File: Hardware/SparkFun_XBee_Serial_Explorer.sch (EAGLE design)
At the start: 45 parts, among them Q1 MBT2222, U1 MAX232SOIC16, U2 XBEE-1B3, U3 LM117

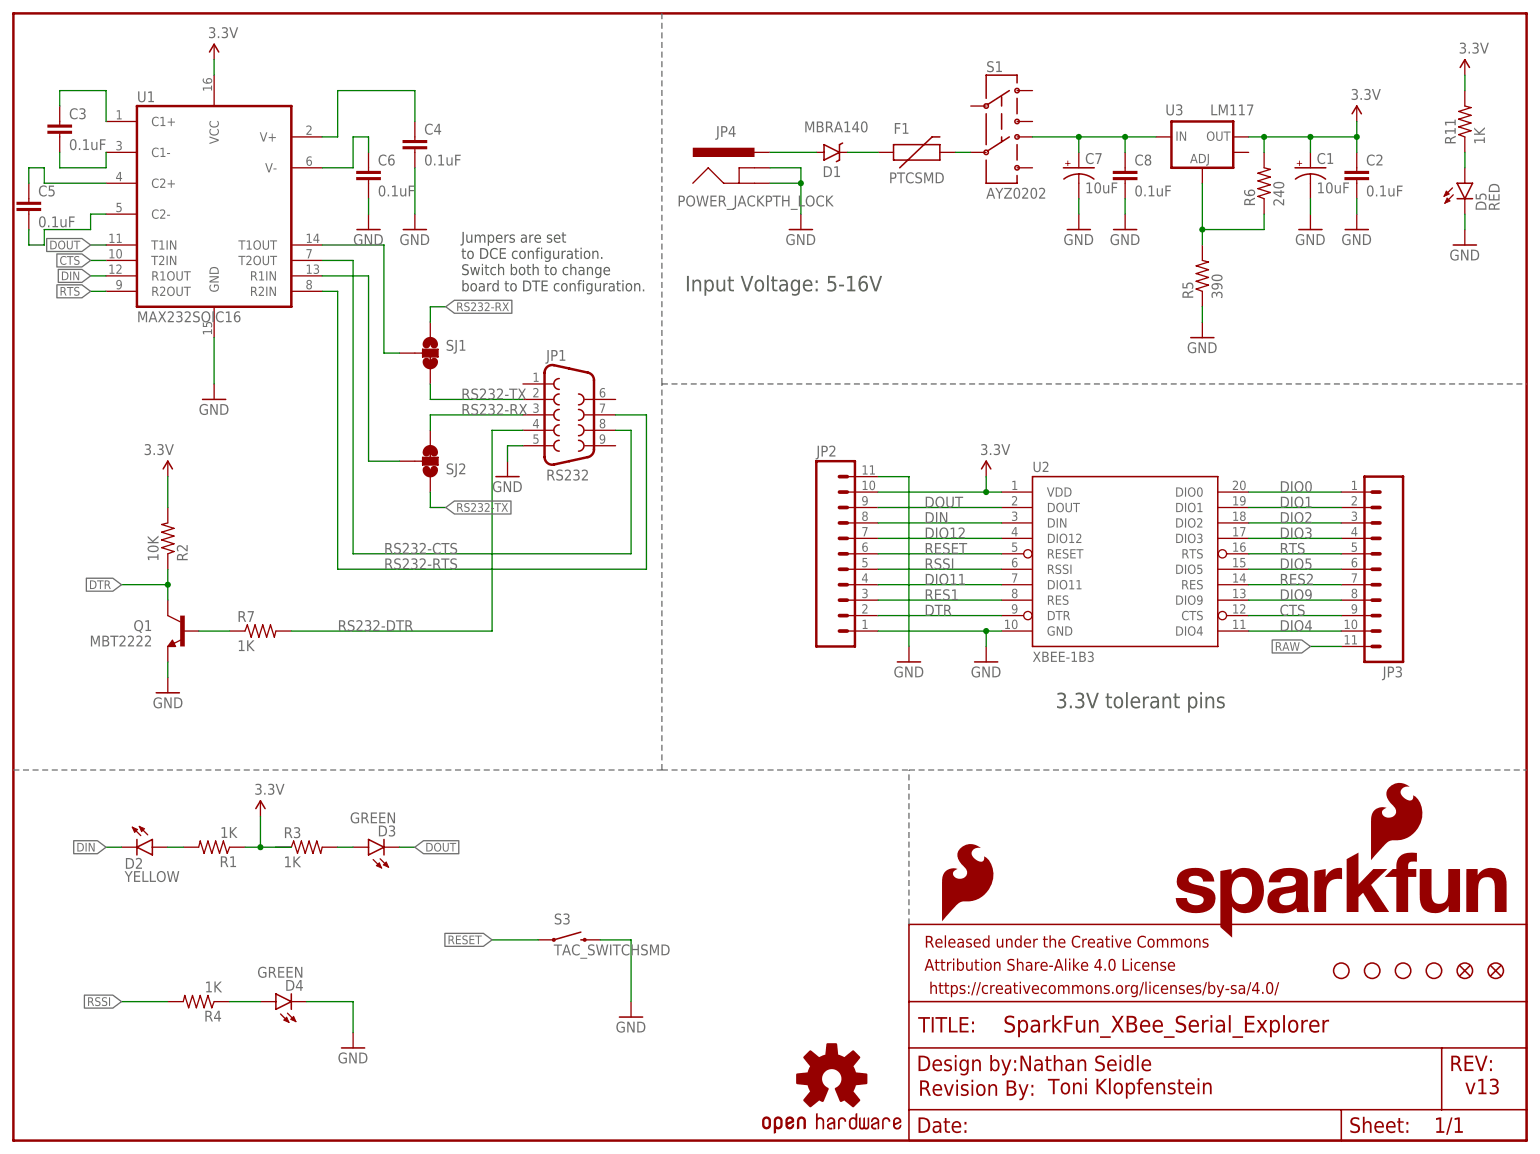
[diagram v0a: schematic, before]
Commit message: Adding in test points for QC
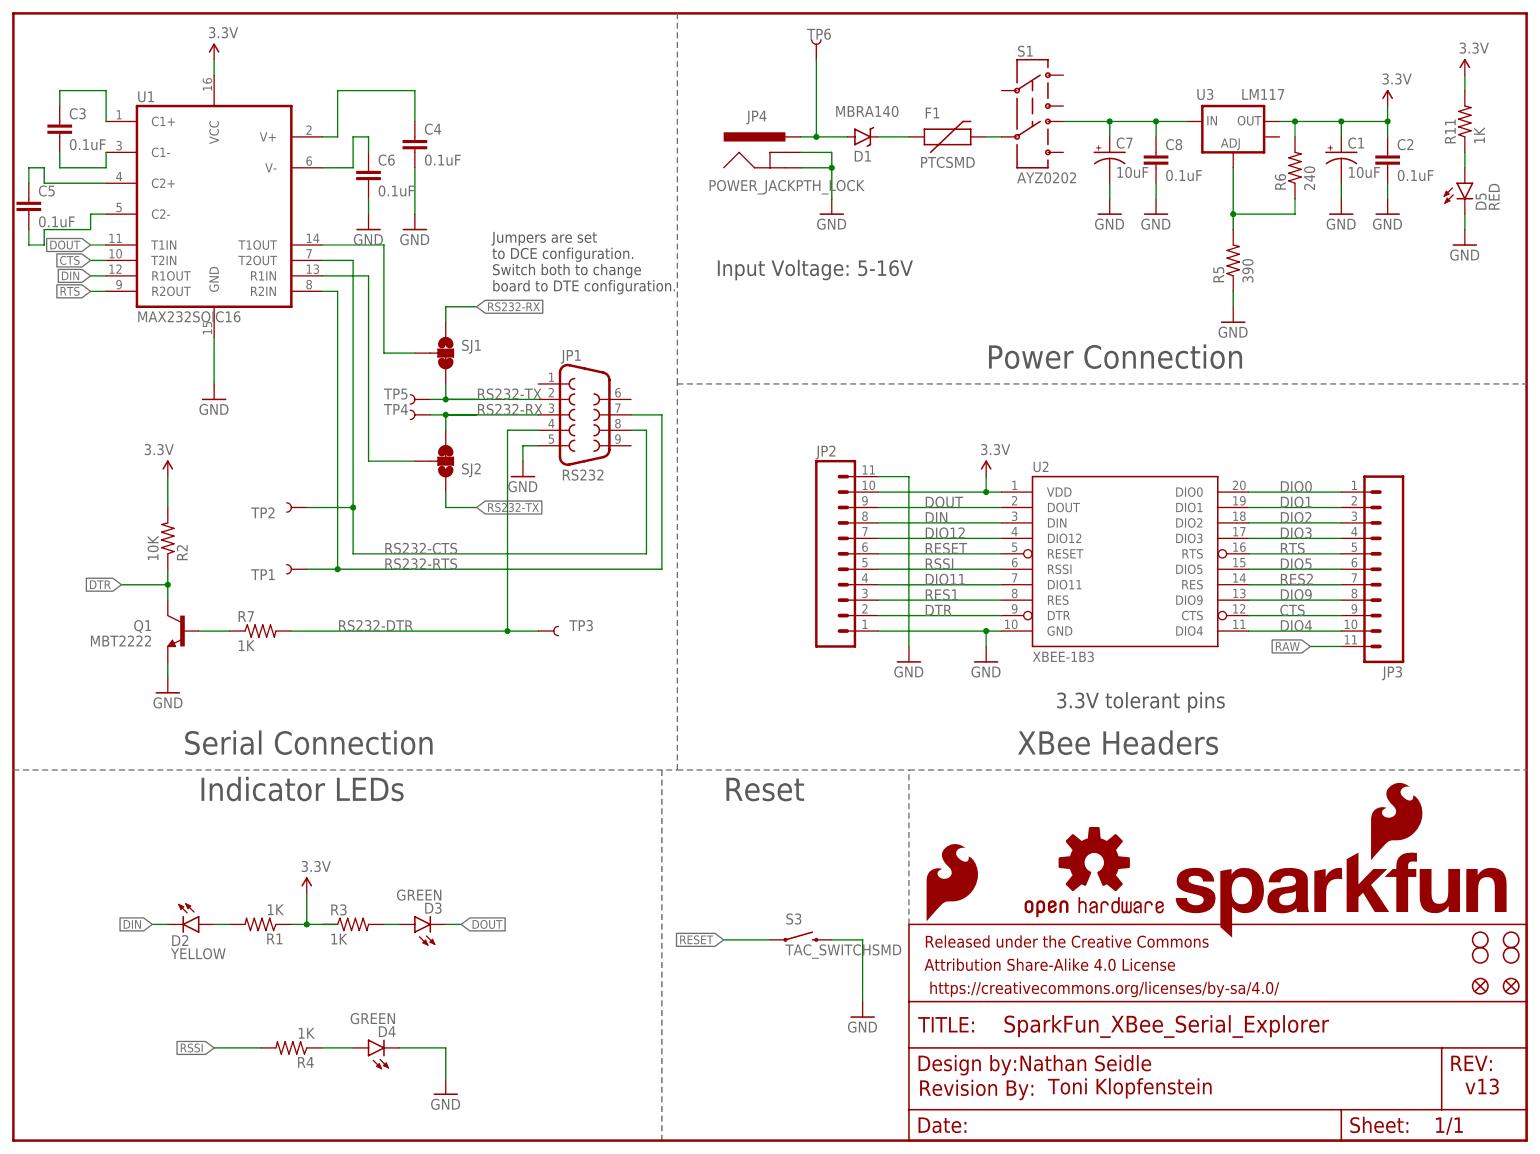
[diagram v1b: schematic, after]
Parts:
- added TP1, TP2, TP3, TP4, TP5, TP6: TEST-POINTTP_15TH_THRU, SparkFun-Passives:TEST-POINTTP_15TH_THRU
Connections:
- net N$15: now also TP6.1
- net RS232-CTS: now also TP2.1
- net RS232-DTR: now also TP3.1
- net RS232-RTS: now also TP1.1
- net RS232-RX: now also TP4.1
- net RS232-TX: now also TP5.1
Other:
- note added: "Indicator LEDs"
- note added: "Power Connection"
- note added: "Reset"
- note added: "Serial Connection"
- note added: "XBee Headers"
- moved on the sheet: C1, C2, C7, C8, D1, D2, D3, D4, F1, JP1, JP4, R1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

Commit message: Fixing PTC part number for proper BOM
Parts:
- F1: value PTCSMD -> PTCTHERMISTOR1206; device SparkFun-PowerIC:PTCSMD -> SparkFun-PowerIC:PTCTHERMISTOR1206
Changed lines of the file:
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@@
 <part name="P+4" library="SparkFun" deviceset="3.3V" device=""/>
 <part name="GND10" library="SparkFun-Aesthetics" deviceset="GND" device=""/>
-<part name="F1" library="SparkFun-PowerIC" deviceset="PTC" device="SMD"/>
+<part name="F1" library="SparkFun-PowerIC" deviceset="PTC" device="THERMISTOR1206" value="PTCTHERMISTOR1206"/>
 <part name="P+5" library="SparkFun" deviceset="3.3V" device=""/>
 <part name="GND11" library="SparkFun" deviceset="GND" device=""/>
@@
 <instance part="P+4" gate="G$1" x="238.76" y="175.26"/>
 <instance part="GND10" gate="1" x="134.62" y="152.4"/>
-<instance part="F1" gate="G$1" x="152.4" y="165.1"/>
+<instance part="F1" gate="G$1" x="152.4" y="165.1" smashed="yes">
+<attribute name="NAME" x="149.86" y="168.148" size="1.778" layer="95"/>
+<attribute name="VALUE" x="165.862" y="162.56" size="1.778" layer="96" rot="R180"/>
+</instance>
 <instance part="P+5" gate="G$1" x="226.06" y="170.18"/>
 <instance part="GND11" gate="1" x="83.82" y="109.22"/>

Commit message: Final QC checklist and changes for testbed
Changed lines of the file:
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@@
 <?xml version="1.0" encoding="utf-8"?>
 <!DOCTYPE eagle SYSTEM "eagle.dtd">
-<eagle version="7.1.0">
+<eagle version="7.2.0">
 <drawing>
 <settings>
@@
 <instance part="JP1" gate="G$1" x="93.98" y="119.38"/>
 <instance part="JP4" gate="G$1" x="127" y="157.48" smashed="yes">
-<attribute name="VALUE" x="114.3" y="156.21" size="1.778" layer="96"/>
 <attribute name="NAME" x="120.65" y="167.64" size="1.778" layer="95"/>
 </instance>
@@
 <instance part="F1" gate="G$1" x="152.4" y="165.1" smashed="yes">
 <attribute name="NAME" x="149.86" y="168.148" size="1.778" layer="95"/>
-<attribute name="VALUE" x="165.862" y="162.56" size="1.778" layer="96" rot="R180"/>
 </instance>
 <instance part="P+5" gate="G$1" x="226.06" y="170.18"/>
@@
 <instance part="R5" gate="G$1" x="200.66" y="144.78" rot="R90"/>
 <instance part="R6" gate="G$1" x="210.82" y="160.02" rot="R90"/>
-<instance part="S3" gate="G$1" x="129.54" y="33.02"/>
+<instance part="S3" gate="G$1" x="129.54" y="33.02" smashed="yes">
+<attribute name="NAME" x="127" y="35.56" size="1.778" layer="95"/>
+</instance>
 <instance part="GND14" gate="1" x="139.7" y="20.32"/>
 <instance part="R7" gate="G$1" x="40.64" y="83.82"/>
@@
 <attribute name="NAME" x="73.66" y="111.379" size="1.778" layer="95" rot="MR180"/>
 </instance>
-<instance part="S1" gate="G$1" x="167.64" y="170.18"/>
+<instance part="S1" gate="G$1" x="167.64" y="170.18" smashed="yes">
+<attribute name="NAME" x="165.1" y="178.308" size="1.778" layer="95"/>
+</instance>
 <instance part="LOGO3" gate="G$1" x="149.86" y="35.56"/>
 <instance part="TP1" gate="G$1" x="48.26" y="93.98" smashed="yes" rot="R180">
@@
 </segment>
 <segment>
-<wire x1="50.8" y1="35.56" x2="53.34" y2="35.56" width="0.1524" layer="91"/>
 <wire x1="50.8" y1="35.56" x2="48.26" y2="35.56" width="0.1524" layer="91"/>
 <wire x1="48.26" y1="40.64" x2="48.26" y2="35.56" width="0.1524" layer="91"/>

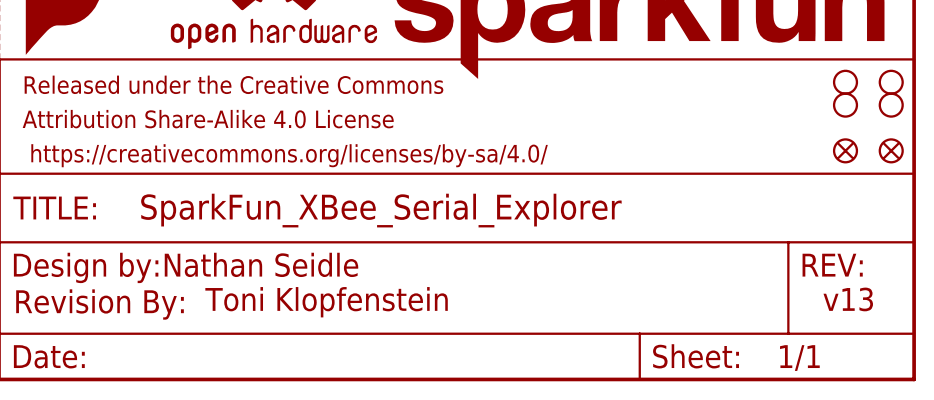
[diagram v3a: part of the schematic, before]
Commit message: Fixing jumper trace, updating version number
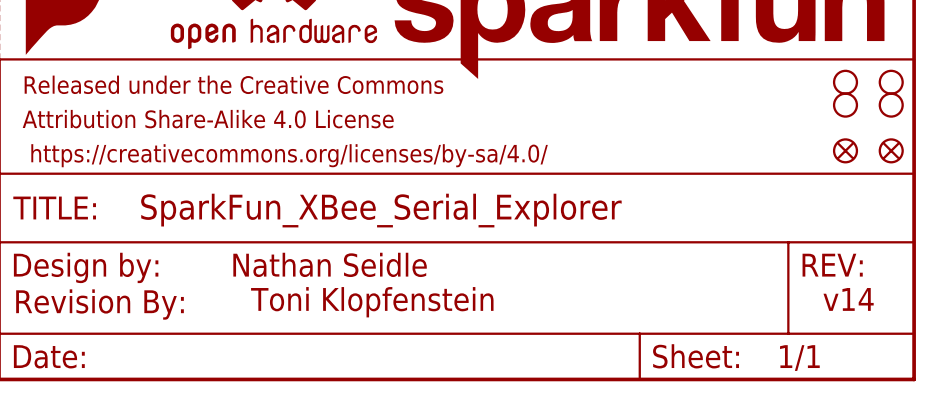
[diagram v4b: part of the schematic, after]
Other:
- note added: "v14"
- note removed: "v13"
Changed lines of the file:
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@@
 <?xml version="1.0" encoding="utf-8"?>
 <!DOCTYPE eagle SYSTEM "eagle.dtd">
-<eagle version="7.2.0">
+<eagle version="7.5.0">
 <drawing>
 <settings>
@@
 <layer number="254" name="cooling" color="7" fill="1" visible="yes" active="yes"/>
 </layers>
-<schematic xreflabel="%F%N/%S.%C%R" xrefpart="/%S.%C%R">
+<schematic xreflabel="%F%N/%S" xrefpart="/%S">
 <attributes>
 </attributes>
@@
 <wire x1="109.22" y1="124.46" x2="248.92" y2="124.46" width="0.1524" layer="95" style="shortdash"/>
 <wire x1="147.32" y1="35.56" x2="147.32" y2="60.96" width="0.1524" layer="95" style="shortdash"/>
-<text x="238.76" y="7.62" size="2.54" layer="94">v13</text>
-<text x="165.354" y="11.43" size="2.54" layer="94">Nathan Seidle</text>
-<text x="170.18" y="7.62" size="2.54" layer="94">Toni Klopfenstein</text>
+<text x="238.76" y="7.62" size="2.54" layer="94">v14</text>
+<text x="172.974" y="11.43" size="2.54" layer="94">Nathan Seidle</text>
+<text x="175.26" y="7.62" size="2.54" layer="94">Toni Klopfenstein</text>
 <text x="78.74" y="139.7" size="1.778" layer="97">Jumpers are set
 to DCE configuration.
